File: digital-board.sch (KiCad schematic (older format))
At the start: 233 parts, among them IC1 ATMEGA6450-A, J1 CONN_20X2, Q1 2N3904, Q2 2N3904, SW15 TACT_SWITCH, SW16 TACT_SWITCH, SW17 TACT_SWITCH, SW18 TACT_SWITCH, SW19 TACT_SWITCH, SW20 TACT_SWITCH, SW21 TACT_SWITCH, SW22 TACT_SWITCH, SW23 TACT_SWITCH, U1 DG419, U10 74LVC1G32, U11 74HC165, U12 74AC595, U13 74AC595, U14 74HC165, U15 74AC595, U16 74AC595, U2 74HC4067, U3 R-78E5.0-1.0, U4 74HC4067, U5 74LS573, U6 74LS573, U7 74LVC2G04, U8 74AC595, U9 74HC165, X1 MIDI OUT, X2 MIDI IN, X3 MIDI THRU

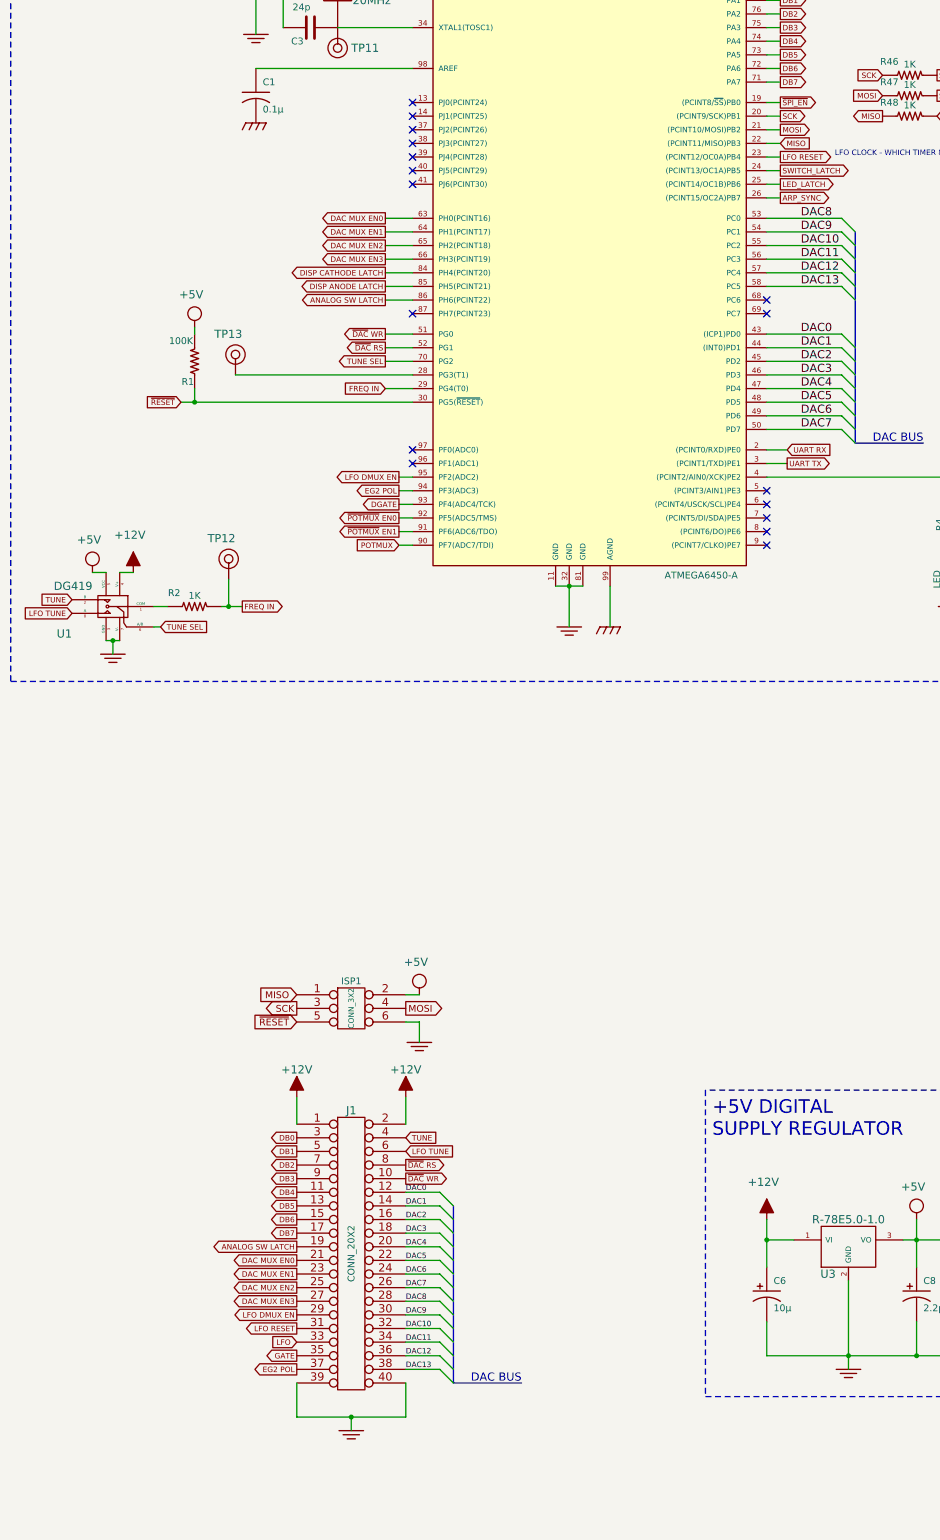
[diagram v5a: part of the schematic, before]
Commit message: working on J1 and MCU connections for optimal routing
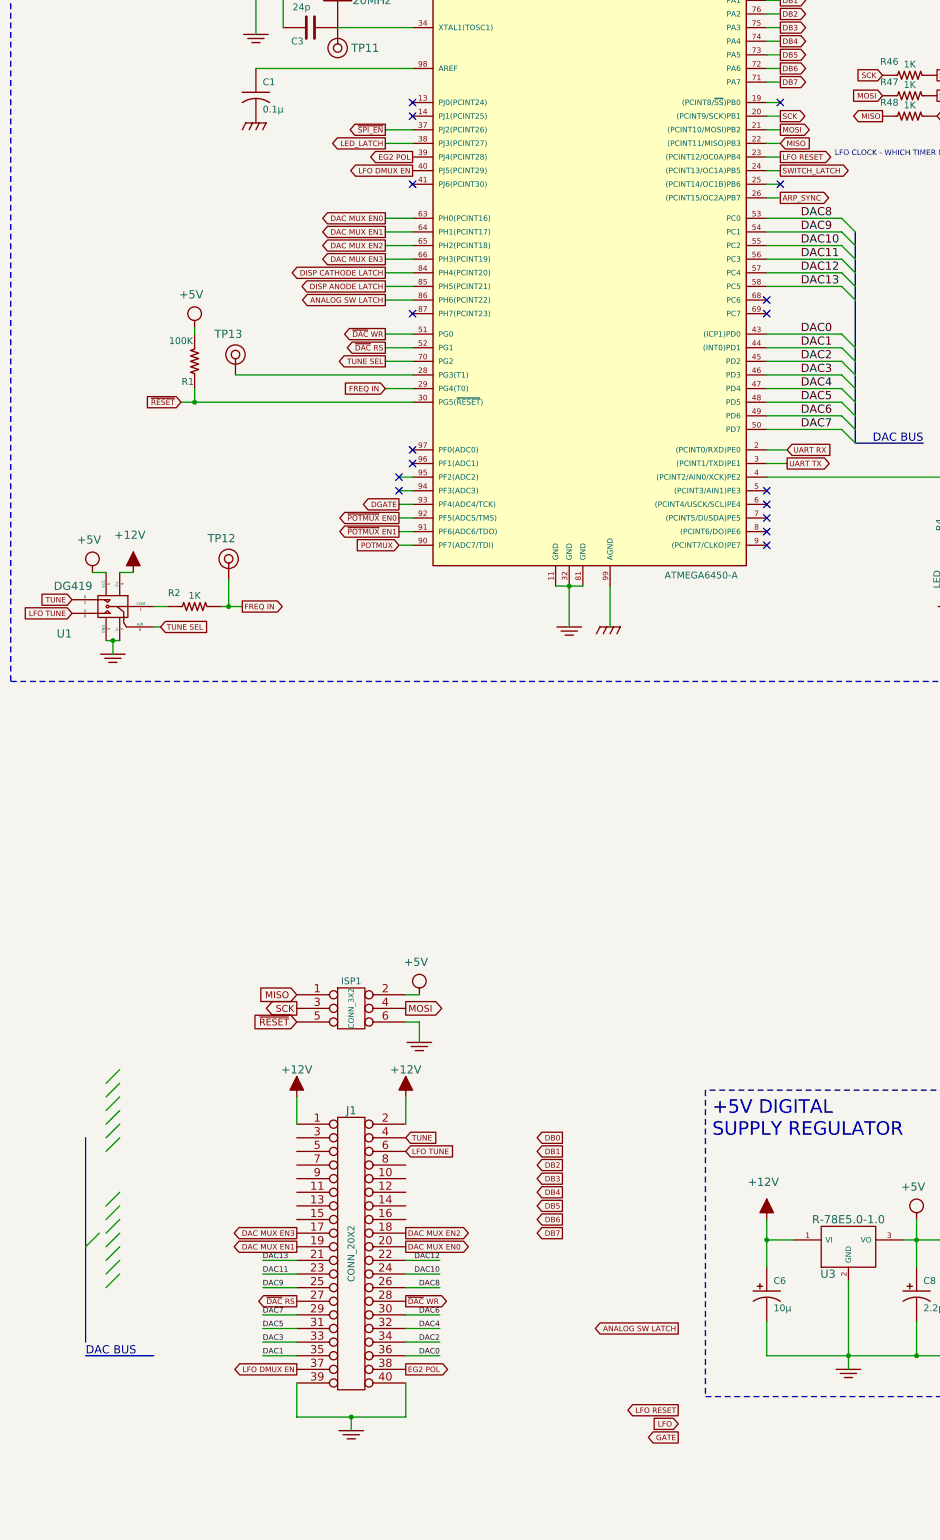
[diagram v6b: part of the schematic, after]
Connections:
- wire segments 933 -> 935
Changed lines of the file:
@@
 	0    -1   -1   0
 $EndComp
-Text GLabel 2700 10550 0    40   Output ~ 0
+Text GLabel 4650 10550 0    40   Output ~ 0
 DB0
-Text GLabel 2700 10650 0    40   Output ~ 0
+Text GLabel 4650 10650 0    40   Output ~ 0
 DB1
-Text GLabel 2700 10750 0    40   Output ~ 0
+Text GLabel 4650 10750 0    40   Output ~ 0
 DB2
-Text GLabel 2700 10850 0    40   Output ~ 0
+Text GLabel 4650 10850 0    40   Output ~ 0
 DB3
-Text GLabel 2700 10950 0    40   Output ~ 0
+Text GLabel 4650 10950 0    40   Output ~ 0
 DB4
-Text GLabel 2700 11050 0    40   Output ~ 0
+Text GLabel 4650 11050 0    40   Output ~ 0
 DB5
-Text GLabel 2700 11150 0    40   Output ~ 0
+Text GLabel 4650 11150 0    40   Output ~ 0
 DB6
-Text GLabel 2700 11250 0    40   Output ~ 0
+Text GLabel 4650 11250 0    40   Output ~ 0
 DB7
-Text GLabel 2700 11350 0    40   Output ~ 0
+Text GLabel 5500 11950 0    40   Output ~ 0
 ANALOG SW LATCH
 Text GLabel 3500 10650 2    40   Input ~ 0
 LFO TUNE
-Text GLabel 2700 12150 0    40   Output ~ 0
+Text GLabel 5500 12750 0    40   Output ~ 0
 GATE
-Text GLabel 2700 11450 0    40   Output ~ 0
+Text GLabel 3500 11350 2    40   Output ~ 0
 DAC MUX EN0
-Text GLabel 2700 11550 0    40   Output ~ 0
+Text GLabel 2700 11350 0    40   Output ~ 0
 DAC MUX EN1
-Text GLabel 2700 11650 0    40   Output ~ 0
+Text GLabel 3500 11250 2    40   Output ~ 0
 DAC MUX EN2
-Text GLabel 2700 11750 0    40   Output ~ 0
+Text GLabel 2700 11250 0    40   Output ~ 0
 DAC MUX EN3
 Text GLabel 3500 10550 2    40   Input ~ 0
 TUNE
-Text GLabel 2700 11850 0    40   Output ~ 0
+Text GLabel 2700 12250 0    40   Output ~ 0
 LFO DMUX EN
-Text GLabel 2700 11950 0    40   Output ~ 0
+Text GLabel 5500 12550 0    40   Output ~ 0
 LFO RESET
-Text GLabel 2700 12050 0    40   Input ~ 0
+Text GLabel 5500 12650 0    40   Input ~ 0
 LFO
 $Comp
@@
 Text Notes 700  800  0    100  ~ 0
 MCU
-Text GLabel 3500 10850 2    40   Output ~ 0
+Text GLabel 3500 11750 2    40   Output ~ 0
 ~DAC WR
-Text GLabel 3500 10750 2    40   Output ~ 0
+Text GLabel 2700 11750 0    40   Output ~ 0
 ~DAC RS
-Text Label 3500 10950 0    40   ~ 0
+Text Label 3750 12150 2    40   ~ 0
 DAC0
-Text Label 3500 11050 0    40   ~ 0
+Text Label 2450 12150 0    40   ~ 0
 DAC1
-Text Label 3500 11150 0    40   ~ 0
+Text Label 3750 12050 2    40   ~ 0
 DAC2
-Text Label 3500 11250 0    40   ~ 0
+Text Label 2450 12050 0    40   ~ 0
 DAC3
-Text Label 3500 11350 0    40   ~ 0
+Text Label 3750 11950 2    40   ~ 0
 DAC4
-Text Label 3500 11450 0    40   ~ 0
+Text Label 2450 11950 0    40   ~ 0
 DAC5
-Text Label 3500 11550 0    40   ~ 0
+Text Label 3750 11850 2    40   ~ 0
 DAC6
-Text Label 3500 11650 0    40   ~ 0
+Text Label 2450 11850 0    40   ~ 0
 DAC7
-Text Label 3500 11750 0    40   ~ 0
+Text Label 3750 11650 2    40   ~ 0
 DAC8
-Text Label 3500 11850 0    40   ~ 0
+Text Label 2450 11650 0    40   ~ 0
 DAC9
-Text Label 3500 11950 0    40   ~ 0
+Text Label 3750 11550 2    40   ~ 0
 DAC10
-Text Label 3500 12050 0    40   ~ 0
+Text Label 2450 11550 0    40   ~ 0
 DAC11
-Text Label 3500 12150 0    40   ~ 0
+Text Label 3750 11450 2    40   ~ 0
 DAC12
-Text Label 3500 12250 0    40   ~ 0
+Text Label 2450 11450 0    40   ~ 0
 DAC13
 Entry Wire Line
-	3850 12250 3750 12150
+	1400 10150 1300 10250
 Entry Wire Line
-	3850 12350 3750 12250
+	1400 10050 1300 10150
 Entry Wire Line
-	3850 11050 3750 10950
+	1400 11550 1300 11650
 Entry Wire Line
-	3850 11150 3750 11050
+	1400 11450 1300 11550
 Entry Wire Line
-	3850 11250 3750 11150
+	1400 11350 1300 11450
 Entry Wire Line
-	3850 11350 3750 11250
+	1400 11250 1300 11350
 Entry Wire Line
-	3850 11450 3750 11350
+	1400 11150 1300 11250
 Entry Wire Line
-	3850 11550 3750 11450
+	1400 11050 1300 11150
 Entry Wire Line
-	3850 11650 3750 11550
+	1400 10950 1300 11050
 Entry Wire Line
-	3850 11750 3750 11650
+	1250 11250 1150 11350
 Entry Wire Line
-	3850 11850 3750 11750
+	1400 10550 1300 10650
 Entry Wire Line
-	3850 11950 3750 11850
+	1400 10450 1300 10550
 Entry Wire Line
-	3850 12050 3750 11950
+	1400 10350 1300 10450
 Entry Wire Line
-	3850 12150 3750 12050
-Text Notes 4350 12350 2    60   ~ 0
+	1400 10250 1300 10350
+Text Notes 1150 12150 0    60   ~ 0
 DAC BUS
 $Comp
@@
 Text GLabel 3350 4100 0    40   Output ~ 0
 DAC MUX EN3
-Text GLabel 3450 5700 0    40   Output ~ 0
+Text GLabel 3550 3450 0    40   Output ~ 0
 LFO DMUX EN
 Text GLabel 3450 5900 0    40   Output ~ 0
 DGATE
-Text GLabel 2700 12250 0    40   Output ~ 0
+Text GLabel 3500 12250 2    40   Output ~ 0
 EG2 POL
-Text GLabel 3450 5800 0    40   Output ~ 0
+Text GLabel 3550 3350 0    40   Output ~ 0
 EG2 POL
 $Comp
@@
 Text GLabel 15800 20700 0    60   Input ~ 0
 ARP_SYNC
-Text GLabel 6250 3550 2    40   Output ~ 0
+Text GLabel 3350 3250 0    40   Output ~ 0
 LED_LATCH
 Text GLabel 6250 3650 2    40   Output ~ 0
@@
 	1    0    0    -1
 $EndComp
-Text GLabel 6250 2950 2    40   Output ~ 0
+Text GLabel 3350 3150 0    40   Output ~ 0
 ~SPI_EN
 $Comp
@@
 	6750 11600 6750 12250
 Wire Bus Line
-	3850 12350 4350 12350
+	1650 12150 1150 12150
 Wire Bus Line
-	3850 11050 3850 12350
+	1150 10550 1150 12050
 Wire Wire Line
-	3750 12250 3500 12250
+	2700 11450 2450 11450
 Wire Wire Line
-	3750 12150 3500 12150
+	3500 11450 3750 11450
 Wire Wire Line
-	3750 12050 3500 12050
+	2700 11550 2450 11550
 Wire Wire Line
-	3750 11950 3500 11950
+	3500 11550 3750 11550
 Wire Wire Line
-	3750 11850 3500 11850
+	2700 11650 2450 11650
 Wire Wire Line
-	3750 11750 3500 11750
+	3500 11650 3750 11650
 Wire Wire Line
-	3750 11650 3500 11650
+	2700 11850 2450 11850
 Wire Wire Line
-	3750 11550 3500 11550
+	3500 11850 3750 11850
 Wire Wire Line
-	3750 11450 3500 11450
+	2700 11950 2450 11950
 Wire Wire Line
-	3750 11350 3500 11350
+	3500 11950 3750 11950
 Wire Wire Line
-	3750 11250 3500 11250
+	2700 12050 2450 12050
 Wire Wire Line
-	3500 11150 3750 11150
+	3750 12050 3500 12050
 Wire Wire Line
-	3500 11050 3750 11050
+	2450 12150 2700 12150
 Wire Wire Line
-	3500 10950 3750 10950
+	3750 12150 3500 12150
 Wire Notes Line
 	8750 600  600  600
@@
 NoConn ~ 3550 2950
 NoConn ~ 3550 3050
-NoConn ~ 3550 3150
-NoConn ~ 3550 3250
-NoConn ~ 3550 3350
-NoConn ~ 3550 3450
 NoConn ~ 3550 3550
+NoConn ~ 3450 5700
+NoConn ~ 3450 5800
+NoConn ~ 6250 3550
+NoConn ~ 6250 2950
 $Comp
 L +5V #PWR0114
@@
 Wire Notes Line
 	15150 19450 15150 19550
+Wire Wire Line
+	3350 3250 3550 3250
+Wire Wire Line
+	3550 3150 3350 3150
 $EndSCHEMATC
